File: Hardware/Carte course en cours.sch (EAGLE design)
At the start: 40 parts, among them J2 AVR_SPI_PROG_3X2NS, J3 PWR IN, J4 RC receiver, J5 ESC, J6 ESC, J7 MICRO-SD_CARD_SOCKET, J8 ESC, U1 V_REG_317SMD, U2 ATMEGA328P_TQFP, U3 FT232RL, U4 MPU6050, Y1 16MHz

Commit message: Route
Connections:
- net +3V3: no longer J2.2
- net +5V: now also J2.2
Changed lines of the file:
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@@
 <part name="+3V33" library="supply1" library_urn="urn:adsk.eagle:library:371" deviceset="+3V3" device=""/>
 <part name="+3V315" library="supply1" library_urn="urn:adsk.eagle:library:371" deviceset="+3V3" device=""/>
-<part name="+3V34" library="supply1" library_urn="urn:adsk.eagle:library:371" deviceset="+3V3" device=""/>
 <part name="+3V35" library="supply1" library_urn="urn:adsk.eagle:library:371" deviceset="+3V3" device=""/>
 <part name="+3V31" library="supply1" library_urn="urn:adsk.eagle:library:371" deviceset="+3V3" device=""/>
@@
 <part name="J8" library="SparkFun-Connectors" library_urn="urn:adsk.eagle:library:513" deviceset="CONN_02" device="" package3d_urn="urn:adsk.eagle:package:38039/1" value="ESC"/>
 <part name="J9" library="SparkFun-Connectors" library_urn="urn:adsk.eagle:library:513" deviceset="CONN_04" device="" package3d_urn="urn:adsk.eagle:package:38085/1"/>
+<part name="P+2" library="supply1" library_urn="urn:adsk.eagle:library:371" deviceset="+5V" device=""/>
 </parts>
 <sheets>
@@
 <instance part="+3V33" gate="G$1" x="71.12" y="167.64"/>
 <instance part="+3V315" gate="G$1" x="256.54" y="147.32" rot="MR0"/>
-<instance part="+3V34" gate="G$1" x="81.28" y="33.02"/>
 <instance part="+3V35" gate="G$1" x="83.82" y="119.38"/>
 <instance part="+3V31" gate="G$1" x="12.7" y="119.38"/>
@@
 <instance part="J8" gate="G$1" x="154.94" y="104.14" rot="MR0"/>
 <instance part="J9" gate="G$1" x="10.16" y="142.24" rot="MR90"/>
+<instance part="P+2" gate="1" x="81.28" y="33.02"/>
 </instances>
 <busses>
@@
 <junction x="15.24" y="162.56"/>
 </segment>
+<segment>
+<pinref part="J2" gate="G$1" pin="2"/>
+<wire x1="71.12" y1="27.94" x2="81.28" y2="27.94" width="0.1524" layer="91"/>
+<wire x1="81.28" y1="27.94" x2="81.28" y2="30.48" width="0.1524" layer="91"/>
+<pinref part="P+2" gate="1" pin="+5V"/>
+</segment>
 </net>
 <net name="+3V3" class="0">
@@
 </segment>
 <segment>
-<pinref part="J2" gate="G$1" pin="2"/>
-<wire x1="71.12" y1="27.94" x2="81.28" y2="27.94" width="0.1524" layer="91"/>
-<wire x1="81.28" y1="27.94" x2="81.28" y2="30.48" width="0.1524" layer="91"/>
-<pinref part="+3V34" gate="G$1" pin="+3V3"/>
-</segment>
-<segment>

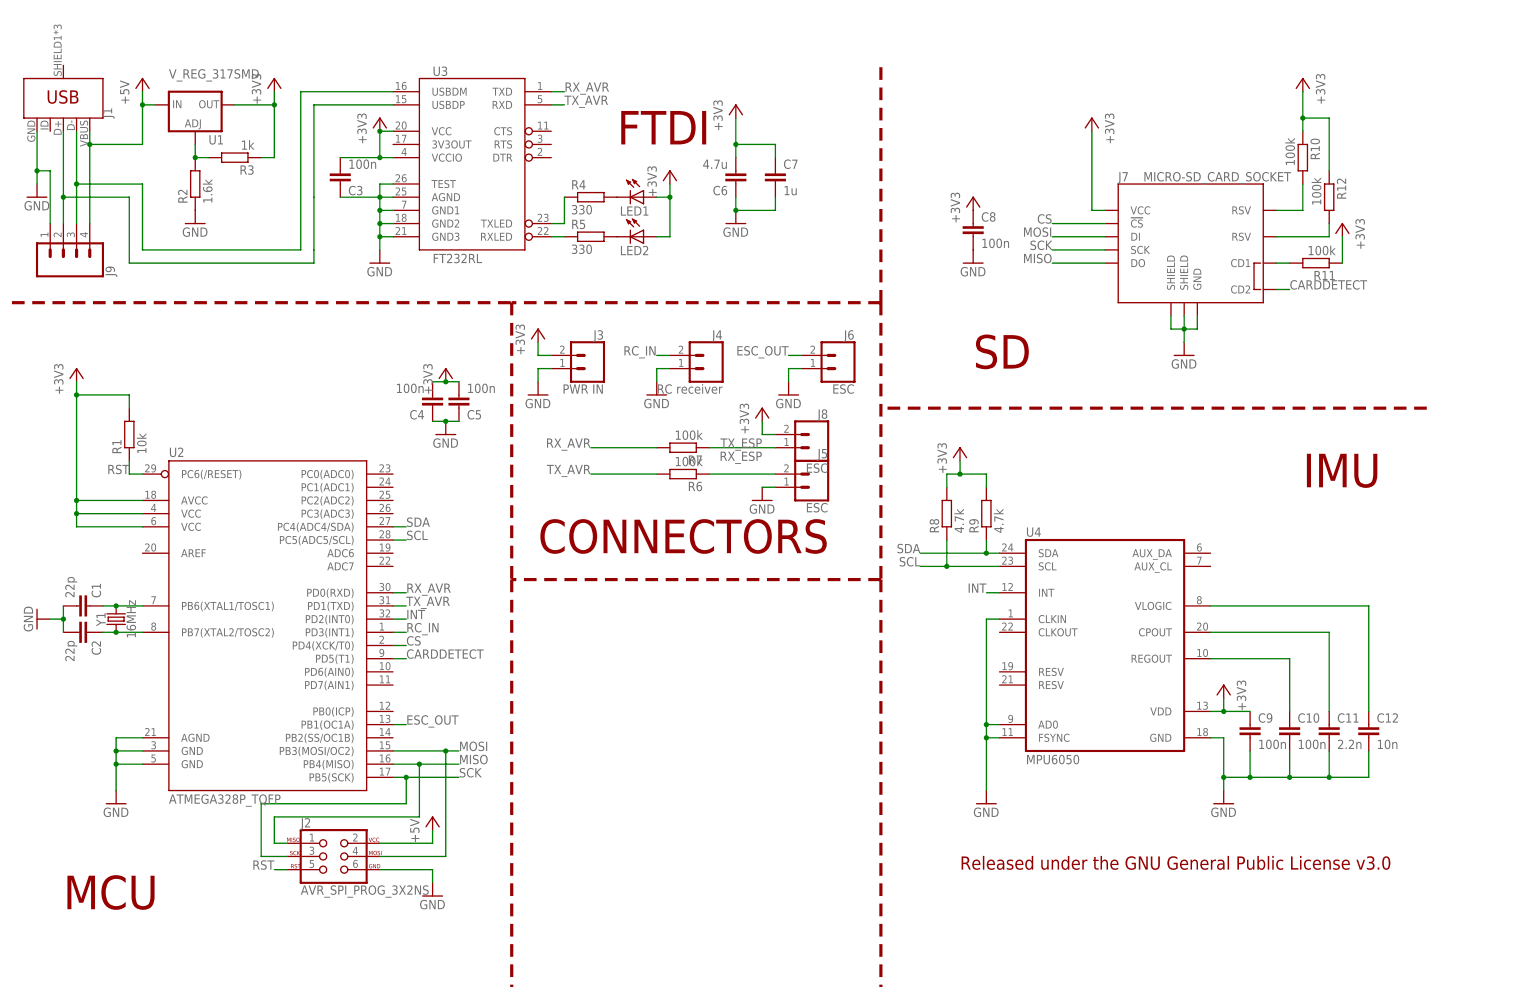
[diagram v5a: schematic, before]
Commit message: Add silkscreen
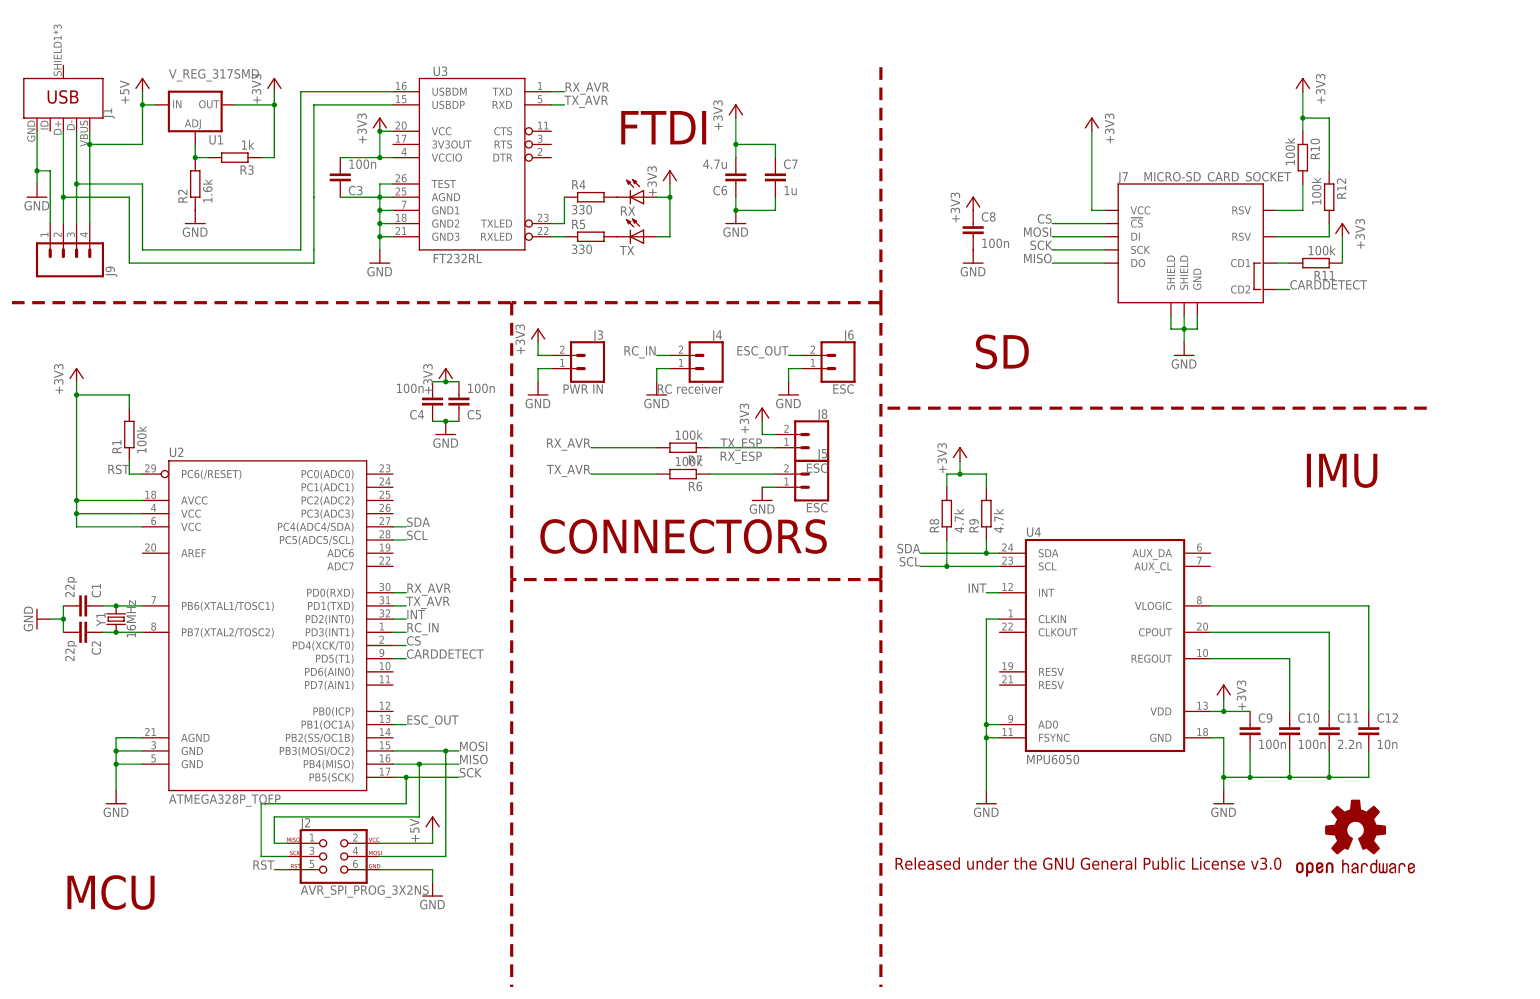
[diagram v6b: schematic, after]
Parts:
- added LOGO1: OSHW-LOGOM, SparkFun-Aesthetics:OSHW-LOGOM
- R1: value 10k -> 100k
- renumbered LED1 to RX, LED2 to TX
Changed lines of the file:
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@@
 <part name="C9" library="rcl" library_urn="urn:adsk.eagle:library:334" deviceset="C-EU" device="C0805" package3d_urn="urn:adsk.eagle:package:23617/2" value="100n"/>
 <part name="C8" library="rcl" library_urn="urn:adsk.eagle:library:334" deviceset="C-EU" device="C0805" package3d_urn="urn:adsk.eagle:package:23617/2" value="100n"/>
-<part name="R1" library="rcl" library_urn="urn:adsk.eagle:library:334" deviceset="R-EU_" device="R0805" package3d_urn="urn:adsk.eagle:package:23553/2" value="10k"/>
+<part name="R1" library="rcl" library_urn="urn:adsk.eagle:library:334" deviceset="R-EU_" device="R0805" package3d_urn="urn:adsk.eagle:package:23553/2" value="100k"/>
 <part name="R9" library="rcl" library_urn="urn:adsk.eagle:library:334" deviceset="R-EU_" device="R0805" package3d_urn="urn:adsk.eagle:package:23553/2" value="4.7k"/>
 <part name="R8" library="rcl" library_urn="urn:adsk.eagle:library:334" deviceset="R-EU_" device="R0805" package3d_urn="urn:adsk.eagle:package:23553/2" value="4.7k"/>
@@
 <part name="R4" library="rcl" library_urn="urn:adsk.eagle:library:334" deviceset="R-EU_" device="R0805" package3d_urn="urn:adsk.eagle:package:23553/2" value="330"/>
 <part name="R5" library="rcl" library_urn="urn:adsk.eagle:library:334" deviceset="R-EU_" device="R0805" package3d_urn="urn:adsk.eagle:package:23553/2" value="330"/>
-<part name="LED1" library="led" library_urn="urn:adsk.eagle:library:259" deviceset="LED" device="CHIPLED_0805" package3d_urn="urn:adsk.eagle:package:15821/1"/>
-<part name="LED2" library="led" library_urn="urn:adsk.eagle:library:259" deviceset="LED" device="CHIPLED_0805" package3d_urn="urn:adsk.eagle:package:15821/1"/>
+<part name="RX" library="led" library_urn="urn:adsk.eagle:library:259" deviceset="LED" device="CHIPLED_0805" package3d_urn="urn:adsk.eagle:package:15821/1"/>
+<part name="TX" library="led" library_urn="urn:adsk.eagle:library:259" deviceset="LED" device="CHIPLED_0805" package3d_urn="urn:adsk.eagle:package:15821/1"/>
 <part name="+3V313" library="supply1" library_urn="urn:adsk.eagle:library:371" deviceset="+3V3" device=""/>
 <part name="GND16" library="supply1" library_urn="urn:adsk.eagle:library:371" deviceset="GND" device=""/>
@@
 <part name="J9" library="SparkFun-Connectors" library_urn="urn:adsk.eagle:library:513" deviceset="CONN_04" device="" package3d_urn="urn:adsk.eagle:package:38085/1"/>
 <part name="P+2" library="supply1" library_urn="urn:adsk.eagle:library:371" deviceset="+5V" device=""/>
+<part name="LOGO1" library="SparkFun-Aesthetics" library_urn="urn:adsk.eagle:library:507" deviceset="OSHW-LOGO" device="M" package3d_urn="urn:adsk.eagle:package:37126/1"/>
 </parts>
 <sheets>
@@
 <text x="248.92" y="96.52" size="6.4516" layer="94" font="vector" ratio="12">IMU</text>
 <text x="116.84" y="162.56" size="6.4516" layer="94" font="vector" ratio="12">FTDI</text>
-<text x="182.88" y="22.86" size="2.54" layer="94" font="vector" ratio="12">Released under the GNU General Public License v3.0</text>
+<text x="170.18" y="22.86" size="2.286" layer="94" font="vector" ratio="12">Released under the GNU General Public License v3.0</text>
 <wire x1="167.64" y1="78.74" x2="96.52" y2="78.74" width="0.6096" layer="94" style="longdash"/>
 <text x="101.6" y="83.82" size="6.4516" layer="94" font="vector" ratio="12">CONNECTORS</text>
@@
 <instance part="R4" gate="G$1" x="111.76" y="152.4"/>
 <instance part="R5" gate="G$1" x="111.76" y="144.78"/>
-<instance part="LED1" gate="G$1" x="121.92" y="152.4" rot="R270"/>
-<instance part="LED2" gate="G$1" x="121.92" y="144.78" rot="R270"/>
+<instance part="RX" gate="G$1" x="121.92" y="152.4" rot="R270"/>
+<instance part="TX" gate="G$1" x="121.92" y="144.78" rot="R270"/>
 <instance part="+3V313" gate="G$1" x="233.68" y="58.42" rot="MR0"/>
 <instance part="GND16" gate="1" x="233.68" y="35.56"/>
@@
 <instance part="J9" gate="G$1" x="10.16" y="142.24" rot="MR90"/>
 <instance part="P+2" gate="1" x="81.28" y="33.02"/>
+<instance part="LOGO1" gate="G$1" x="259.08" y="30.48"/>
 </instances>
 <busses>
@@
 </segment>
 <segment>
-<pinref part="LED1" gate="G$1" pin="A"/>
+<pinref part="RX" gate="G$1" pin="A"/>
 <wire x1="124.46" y1="152.4" x2="127" y2="152.4" width="0.1524" layer="91"/>
-<pinref part="LED2" gate="G$1" pin="A"/>
+<pinref part="TX" gate="G$1" pin="A"/>
 <wire x1="124.46" y1="144.78" x2="127" y2="144.78" width="0.1524" layer="91"/>
 <wire x1="127" y1="144.78" x2="127" y2="152.4" width="0.1524" layer="91"/>
@@
 <segment>
 <pinref part="R4" gate="G$1" pin="2"/>
-<pinref part="LED1" gate="G$1" pin="C"/>
+<pinref part="RX" gate="G$1" pin="C"/>
 </segment>
 </net>
@@
 <segment>
 <pinref part="R5" gate="G$1" pin="2"/>
-<pinref part="LED2" gate="G$1" pin="C"/>
-</segment>
-</net>
+<pinref part="TX" gate="G$1" pin="C"/>
+</segment>
+</net>

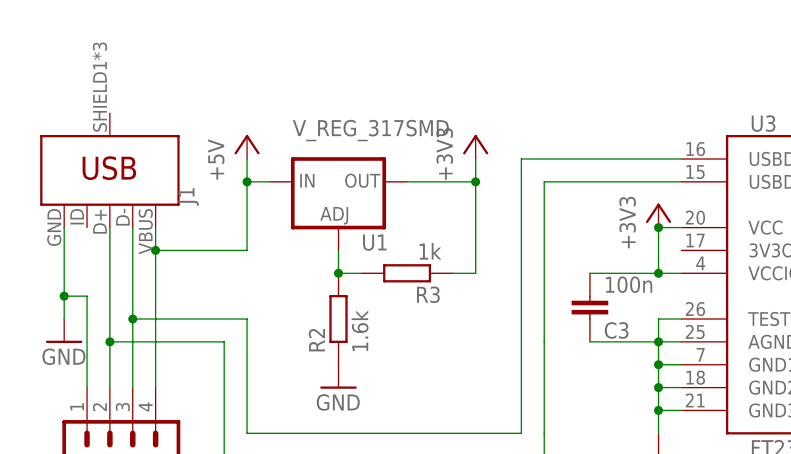
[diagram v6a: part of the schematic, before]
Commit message: Add heatsink plane
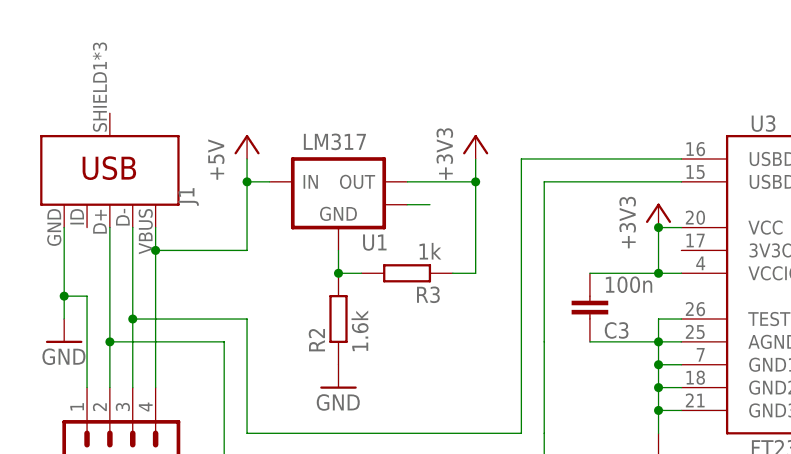
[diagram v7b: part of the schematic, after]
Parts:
- U1: value V_REG_317SMD -> LM317; device SparkFun-IC-Power:V_REG_317SMD -> bt_regulator:LM1117-SOT223
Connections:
- new net HEATSINK: U1.HEATSINK
- net +3V3: now also U1.VOUT; no longer U1.OUT
- net +5V: now also U1.VIN; no longer U1.IN
- net N$1: now also U1.GND; no longer U1.ADJ
